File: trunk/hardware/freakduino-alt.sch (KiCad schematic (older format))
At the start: 10 parts, among them U6 ATMEGA328-QFP32

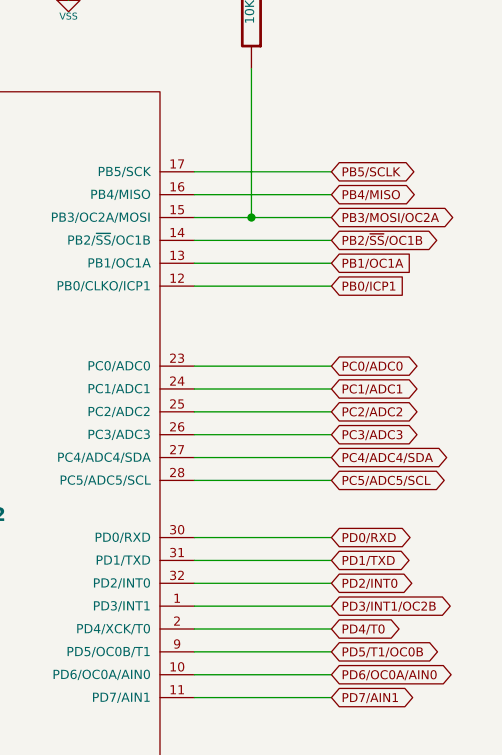
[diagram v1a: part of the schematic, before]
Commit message: Numberous more problems with the circuit design and PCB layout errors found and corrected as a result of debugging and making the RF section work, today, finally.
There remains and issue with the SPI port disable jumper not working as it should -- I think.  I got around this by fluke, when I realised that holding down the reset button (somehow) enables my AVR ISP mkII to program the AVR chip, despite the suspected SPI bus conflict between the ISP and level shofter chip. (Not that any of that makes sense to me right now. But that's what seemed to be the case, at the time. I'll sort it later.)
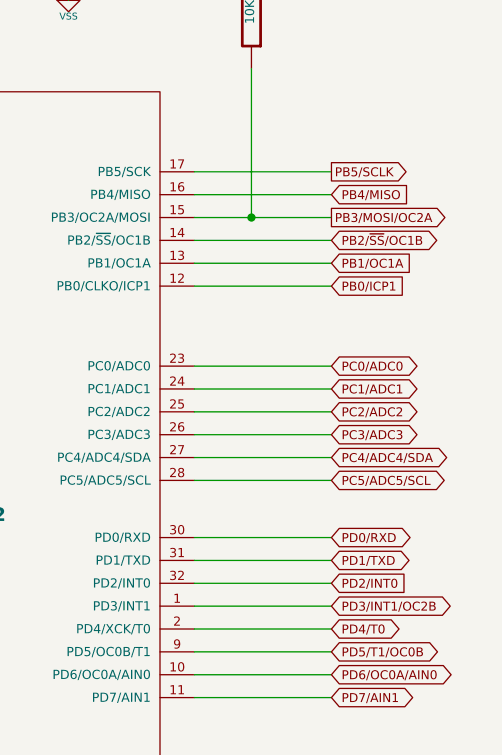
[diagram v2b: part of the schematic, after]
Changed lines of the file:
@@
 Sheet 1 6
 Title "FREAKDUINO-CHIBI 2.4GHz v2.1a compat"
-Date "13 aug 2013"
+Date "16 aug 2013"
 Rev "v1.1"
 Comp "KiCAD version by Gruvin"
@@
 	5550 2700 6000 2700
 Connection ~ 6000 2700
-Text GLabel 9400 3150 2    39   BiDi ~ 0
+Text GLabel 9400 3150 2    39   Output ~ 0
 PB5/SCLK
-Text GLabel 9400 3250 2    39   BiDi ~ 0
+Text GLabel 9400 3250 2    39   Input ~ 0
 PB4/MISO
-Text GLabel 9400 3350 2    39   BiDi ~ 0
+Text GLabel 9400 3350 2    39   Output ~ 0
 PB3/MOSI/OC2A
 Text GLabel 9400 3450 2    39   BiDi ~ 0
@@
 Text GLabel 9400 4850 2    39   BiDi ~ 0
 PD1/TXD
-Text GLabel 9400 4950 2    39   BiDi ~ 0
+Text GLabel 9400 4950 2    39   Input ~ 0
 PD2/INT0
 Text GLabel 9400 5050 2    39   BiDi ~ 0
